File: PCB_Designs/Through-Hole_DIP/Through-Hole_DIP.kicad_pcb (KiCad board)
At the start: 2 copper layers, 46.9 x 22.6 mm, 12 parts, among them J1 USB-AM-S-X-X-TH, U1 ATtiny85-20P, Y1 12MHz

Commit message: Modified
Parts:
- added C3: 0.1uF, Capacitor_THT:C_Disc_D5.0mm_W2.5mm_P5.00mm, F.Cu at (131.3, 94.6)
- moved R3 1.93 mm to (125.2, 89.4)
- moved C2 1.79 mm to (117.9, 84.6)
- moved R4 1.57 mm to (125.3, 99.4)
- moved C1 1.54 mm to (118.0, 100.1)
- moved Y1 1.29 mm to (121.1, 89.8)
- moved D1 1.09 mm to (114.2, 88.9)
- moved D2 1.06 mm to (114.1, 95.3)
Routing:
- net GND: track 83.5 -> 0.00 mm
- net +5V: track 61.5 -> 0.00 mm
- net /Data+: track 42.0 -> 0.00 mm
- net Net-(U1-XTAL2/PB4): track 38.8 -> 0.00 mm
- net Net-(U1-XTAL1/PB3): track 35.5 -> 0.00 mm
- net Net-(U1-PB2): track 15.6 -> 0.00 mm
- net Net-(U1-~{RESET}/PB5): track 15.6 -> 0.00 mm
- net Net-(D1-A): track 12.6 -> 0.00 mm
- net /Data-: track 12.3 -> 0.00 mm
- net Net-(D2-A): track 11.4 -> 0.00 mm
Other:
- outline, holes or cut-outs redrawn

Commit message: Modified
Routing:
- net GND: track 0.00 -> 85.9 mm, vias 0 -> 4
- net +5V: track 0.00 -> 67.4 mm, vias 0 -> 2
- net Net-(U1-XTAL2/PB4): track 0.00 -> 38.7 mm
- net /Data+: track 0.00 -> 36.4 mm
- net Net-(U1-XTAL1/PB3): track 0.00 -> 34.4 mm
- net Net-(U1-PB2): track 0.00 -> 15.6 mm
- net Net-(U1-~{RESET}/PB5): track 0.00 -> 15.6 mm
- net /Data-: track 0.00 -> 13.7 mm
- net Net-(D1-A): track 0.00 -> 13.7 mm
- net Net-(D2-A): track 0.00 -> 11.0 mm

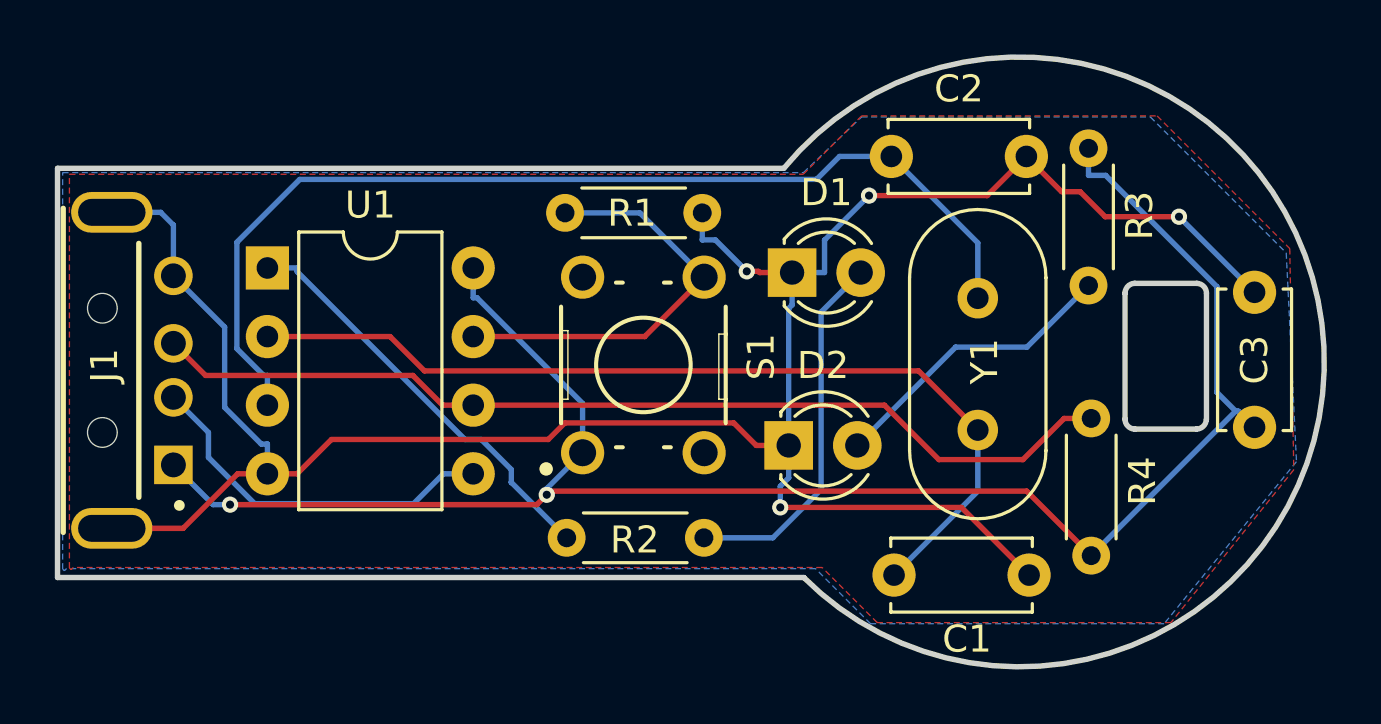
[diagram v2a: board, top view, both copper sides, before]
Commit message: Reposition LEDs on PCB for 3D enclosure alignment
Moved LEDs to new positions on the PCB to ensure proper fit and alignment with the 3D enclosure design. This adjustment accommodates the enclosure's dimensions and improves overall integration.
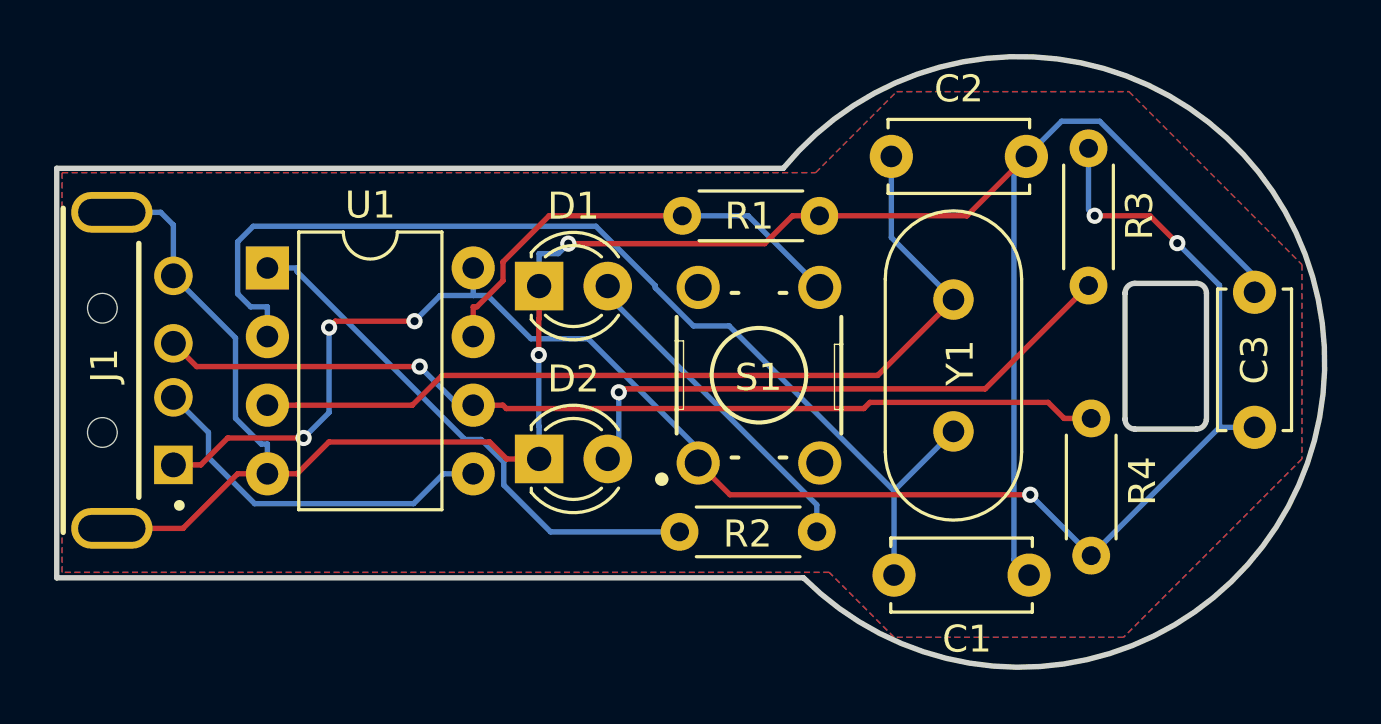
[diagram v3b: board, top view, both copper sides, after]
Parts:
- moved D1 9.38 mm to (104.9, 89.4)
- moved D2 9.25 mm to (104.9, 95.8)
- moved R1 4.34 mm to (110.2, 86.8)
- moved S1 4.30 mm to (113.0, 92.7)
- moved R2 4.19 mm to (110.1, 98.5)
- moved Y1 0.90 mm to (120.2, 89.9)
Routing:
- net Net-(D2-A): track 11.0 -> 21.7 mm, vias 0 -> 1
- net Net-(U1-XTAL2/PB4): track 38.7 -> 33.3 mm
- net Net-(U1-XTAL1/PB3): track 34.4 -> 39.2 mm
- net Net-(U1-~{RESET}/PB5): track 15.6 -> 19.9 mm
- net +5V: track 67.4 -> 65.3 mm, vias 2 -> 6
- net Net-(D1-A): track 13.7 -> 12.3 mm
- net Net-(U1-PB2): track 15.6 -> 16.8 mm
- net /Data+: track 36.4 -> 35.3 mm, vias 0 -> 1
- net GND: track 85.9 -> 85.7 mm, vias 4 -> 2
- added copper zone on B.Cu, net +5V
- added copper zone on F.Cu, net GND
- removed copper zone on F.Cu, net +5V
- removed copper zone on B.Cu, net GND
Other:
- outline, holes or cut-outs redrawn
